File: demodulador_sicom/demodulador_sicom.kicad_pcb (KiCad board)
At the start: 2 copper layers, 50 x 50 mm, 33 parts, among them J1 POWER, J2 OUTPUT, J3 CARRIER_IN, J4 SSB_IN, U1 MC1496D, U2 L7812

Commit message: Update pcb layout.
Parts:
- added H1: MountingHole, MountingHole:MountingHole_3.2mm_M3, F.Cu at (142.3, 119.4)
- added H2: MountingHole, MountingHole:MountingHole_3.2mm_M3, F.Cu at (153.8, 92.3)
- added H3: MountingHole, MountingHole:MountingHole_3.2mm_M3, F.Cu at (183.3, 106.6)
- moved R1 31.3 mm to (146.1, 110.0)
- moved D1 29.5 mm to (139.6, 111.4), turned to 0 degrees
- moved C12 22.4 mm to (150.6, 104.5)
- moved C3 15.2 mm to (152.1, 100.3), turned to 90 degrees
- moved J1 12.9 mm to (140.7, 94.5), turned to 0 degrees
- moved C13 8.57 mm to (142.5, 104.5), turned to 0 degrees
- moved C2 7.54 mm to (141.3, 100.3), turned to 90 degrees
- moved C8 6.56 mm to (173.6, 103.3), turned to 0 degrees
- moved C6 6.32 mm to (163.7, 120.9), turned to 0 degrees
- moved R11 6.25 mm to (172.6, 106.5)
- moved U2 5.94 mm to (146.5, 96.7), turned to 90 degrees
- moved C9 5.70 mm to (172.6, 99.6)
- moved C7 5.60 mm to (173.6, 109.5), turned to 0 degrees
- moved R3 1.86 mm to (171.5, 119.8)
- moved C4 1.80 mm to (152.4, 113.4)
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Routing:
- net +12V: track 9.33 -> 70.8 mm, vias 0 -> 2
- net /V_IN: track 0.00 -> 15.2 mm
- net /OUTPUT: track 14.8 -> 9.38 mm
- net GND: track 0.00 -> 3.67 mm, vias 0 -> 29
- net Net-(D1-A): track 0.00 -> 3.52 mm
- net /OUPUT_B: track 8.25 -> 9.65 mm
- net /CARRIER_A: track 7.27 -> 6.30 mm
- net Net-(C6-Pad1): track 5.83 -> 6.55 mm
- net /OUTPUT_A: track 4.97 -> 4.41 mm
- added copper zone on B.Cu, net GND
- added copper zone on F.Cu, net GND
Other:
- board size 50 x 50 mm -> 50 x 35 mm

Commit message: Fix missing connection.
- Add RP diode.
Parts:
- added D2: 1N4007, Diode_SMD:D_SMA_Handsoldering, F.Cu at (139.0, 101.9)
- moved C3 4.67 mm to (150.3, 104.6), turned to 0 degrees
- moved C12 3.86 mm to (147.6, 107.0), turned to 0 degrees
- moved R5 3.57 mm to (159.0, 108.4), turned to 0 degrees
- moved C13 2.53 mm to (145.0, 104.5), turned to 180 degrees
- moved C11 1.52 mm to (162.9, 106.9)
- moved C4 0.97 mm to (152.2, 112.5)
- moved R10 0.97 mm to (159.0, 116.2)
- moved R13 0.97 mm to (159.0, 110.7)
- moved R4 0.97 mm to (155.9, 113.5)
- moved C1 0.97 mm to (154.7, 118.4)
- moved C5 0.97 mm to (149.2, 116.3)
- moved R2 0.97 mm to (159.0, 112.9)
- moved R6 0.97 mm to (152.7, 110.1)
- moved R7 0.97 mm to (152.7, 114.8)
- moved R8 0.97 mm to (151.7, 118.8)
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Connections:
- C5 pad 1: Net-(C5-Pad1) -> Net-(U1-IN_CARRIER)
- J1 pad 1: /V_IN -> Net-(D2-A)
- R7 pad 2: Net-(C5-Pad1) -> Net-(U1-IN_CARRIER)
- R8 pad 2: Net-(C5-Pad1) -> Net-(U1-IN_CARRIER)
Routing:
- net Net-(U1-IN_CARRIER): track 2.90 -> 34.8 mm
- net +12V: track 70.8 -> 60.8 mm, vias 2 -> 3
- net /SSB_A: track 12.1 -> 6.12 mm
- net /V_IN: track 15.2 -> 9.54 mm
- net Net-(D2-A): track 0.00 -> 5.60 mm
- net Net-(C5-Pad1): track 5.46 -> 0.00 mm
- net Net-(C4-Pad1): track 8.89 -> 12.5 mm
- net GND: track 3.67 -> 2.01 mm
- net /SSB: track 7.76 -> 9.30 mm
- net Net-(U1-GAIN_ADJ_2): track 2.81 -> 3.43 mm
- net Net-(U1-GAIN_ADJ): track 3.18 -> 3.79 mm
- net Net-(C6-Pad1): track 6.55 -> 7.06 mm

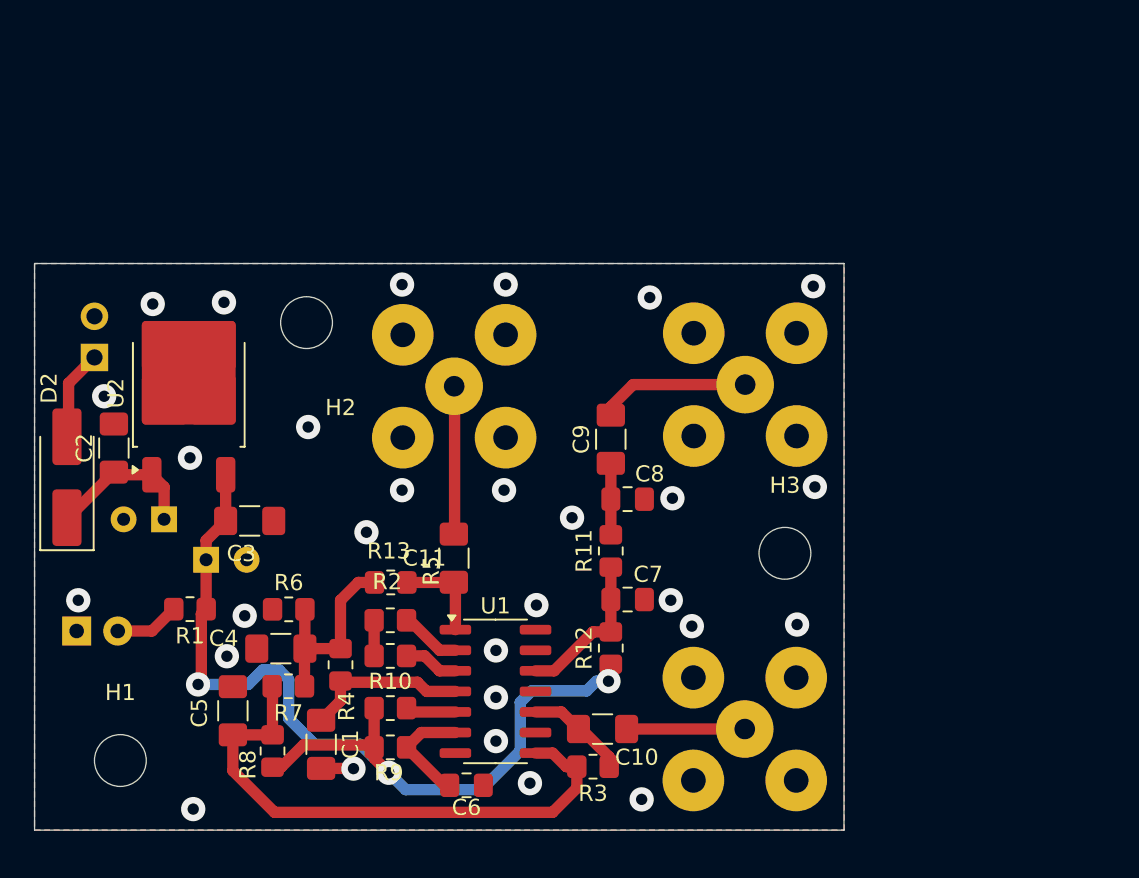
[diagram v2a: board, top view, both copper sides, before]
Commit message: Change BNC footprint.
- Replace vias for holes, so they can have thermal relief.
- Export fabrication files
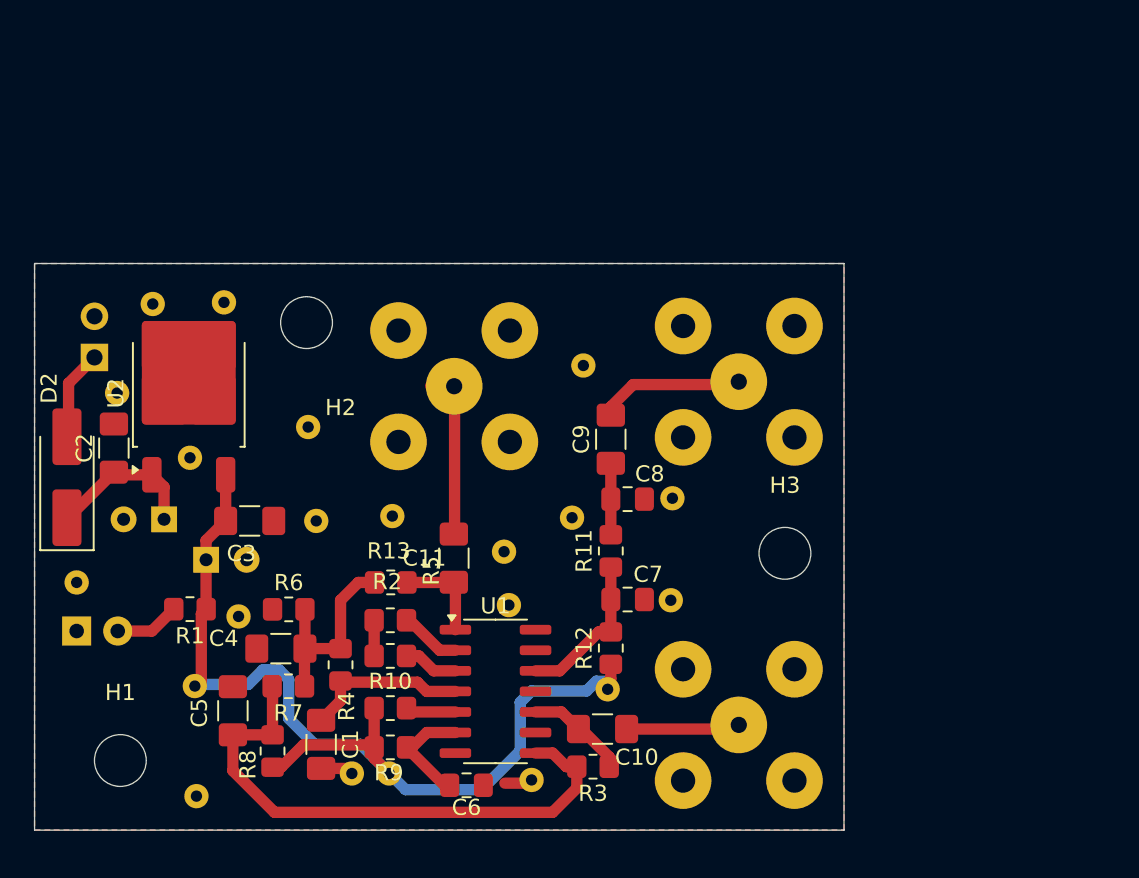
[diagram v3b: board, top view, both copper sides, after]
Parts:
- added H4: ~, via:Via_0.7x1.5, F.Cu at (156.6, 120.2)
- added H4: ~, via:Via_0.7x1.5, F.Cu at (176.3, 109.5)
- added H4: ~, via:Via_0.7x1.5, F.Cu at (147.0, 121.6)
- added H4: ~, via:Via_0.7x1.5, F.Cu at (154.4, 104.6)
- added H4: ~, via:Via_0.7x1.5, F.Cu at (142.1, 96.7)
- added H4: ~, via:Via_0.7x1.5, F.Cu at (176.4, 103.2)
- added H4: ~, via:Via_0.7x1.5, F.Cu at (144.3, 91.2)
- added H4: ~, via:Via_0.7x1.5, F.Cu at (170.9, 95.0)
- added H4: ~, via:Via_0.7x1.5, F.Cu at (139.6, 108.4)
- added H4: ~, via:Via_0.7x1.5, F.Cu at (159.1, 104.3)
- added H4: ~, via:Via_0.7x1.5, F.Cu at (170.2, 104.4)
- added H4: ~, via:Via_0.7x1.5, F.Cu at (167.7, 120.6)
- added H4: ~, via:Via_0.7x1.5, F.Cu at (148.7, 91.1)
- added H4: ~, via:Via_0.7x1.5, F.Cu at (166.3, 109.8)
- added H4: ~, via:Via_0.7x1.5, F.Cu at (149.6, 110.5)
- added H4: ~, via:Via_0.7x1.5, F.Cu at (153.9, 98.8)
- added H4: ~, via:Via_0.7x1.5, F.Cu at (166.0, 106.5)
- added H4: ~, via:Via_0.7x1.5, F.Cu at (146.6, 100.7)
- added H5: ~, via:Via_0.7x1.5, F.Cu at (172.4, 115.0)
- added H5: ~, via:Via_0.7x1.5, F.Cu at (158.9, 120.2)
- added H5: ~, via:Via_0.7x1.5, F.Cu at (146.9, 114.8)
- J2, J3, J4: footprint Connector_Coaxial:BNC_TEConnectivity_1478204_Vertical -> connector:BNC_TEConnectivity_413969-2
- moved J3 0.45 mm to (180.5, 117.2)
- moved J2 0.43 mm to (180.5, 96.0)
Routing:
- net GND: track 2.01 -> 3.76 mm, vias 29 -> 0
- net +12V: vias 3 -> 0

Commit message: Update latest changes.
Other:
- board text added: "DEMO BOTTOM"
- board text added: "DEMO TOP"
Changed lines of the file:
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@@
 		(allow_soldermask_bridges_in_footprints no)
 		(pcbplotparams
-			(layerselection 0x00010c0_ffffffff)
+			(layerselection 0x0001040_7ffffffe)
 			(plot_on_all_layers_selection 0x0000000_00000000)
 			(disableapertmacros no)
@@
 			(outputformat 5)
 			(mirror no)
-			(drillshape 1)
+			(drillshape 0)
 			(scaleselection 1)
 			(outputdirectory "fabrication/svg/")
@@
 		(fp_arc
 			(start 4.76359 -1.712662)
-			(mid 5.062075 0.019867)
+			(mid 5.062075 0.019868)
 			(end 4.750001 1.750001)
 			(stroke
@@
 		(fp_arc
 			(start 4.76359 -1.712662)
-			(mid 5.062075 0.019867)
+			(mid 5.062075 0.019868)
 			(end 4.750001 1.750001)
 			(stroke
@@
 		(fp_arc
 			(start 4.76359 -1.712662)
-			(mid 5.062075 0.019867)
+			(mid 5.062075 0.019868)
 			(end 4.750001 1.750001)
 			(stroke
@@
 		(layer "Edge.Cuts")
 	)
+	(gr_text "DEMO TOP"
+		(at 188.2 106.4 0)
+		(layer "F.Cu")
+		(effects
+			(font
+				(size 1.5 1.5)
+				(thickness 0.3)
+				(bold yes)
+			)
+			(justify left bottom)
+		)
+	)
+	(gr_text "DEMO BOTTOM"
+		(at 203.2 106.2 0)
+		(layer "B.Cu")
+		(effects
+			(font
+				(size 1.5 1.5)
+				(thickness 0.3)
+				(bold yes)
+			)
+			(justify left bottom mirror)
+		)
+	)
 	(dimension
